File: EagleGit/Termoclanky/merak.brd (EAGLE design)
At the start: 160 x 100 mm, 14 parts

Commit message: Termoclanky: - koncept pcb
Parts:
- C1, C2, C5: device rcl:C050-035X075 -> rcl:C0805
- R1, R2, R3: device resistor:0207/12 -> resistor:R0805
- moved LED1 42.4 mm to (7.62, 59.7), turned to 270 degrees
- moved LED2 42.1 mm to (7.62, 54.6), turned to 270 degrees
- moved X2 15.9 mm to (35.6, 59.7), turned to 0 degrees
- moved R3 13.5 mm to (29.2, 48.3), flipped to the bottom, turned to 90 degrees
- moved C1 12.0 mm to (34.3, 40.6), flipped to the bottom
- moved R1 12.0 mm to (30.5, 33.0), flipped to the bottom, turned to 180 degrees
- moved R2 8.13 mm to (31.8, 48.3), flipped to the bottom, turned to 90 degrees
- moved C2 8.03 mm to (38.1, 33.0), flipped to the bottom, turned to 180 degrees
- moved C5 2.84 mm to (36.8, 48.3), flipped to the bottom, turned to 90 degrees
- moved C3 2.84 mm to (54.6, 47.0)
- moved C4 2.84 mm to (54.6, 35.6)
- moved X1 2.84 mm to (68.6, 40.6)
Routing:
- net GND: track 0.00 -> 125.9 mm, vias 0 -> 2
- net VDD: track 0.00 -> 112.3 mm
- net N$1: track 0.00 -> 37.1 mm
- net VSS: track 0.00 -> 33.2 mm
- net N$5: track 0.00 -> 28.9 mm
- net N$6: track 0.00 -> 24.2 mm
- net N$2: track 10.2 -> 16.1 mm
- net N$7: track 0.00 -> 2.86 mm
- net N$4: track 0.00 -> 2.86 mm

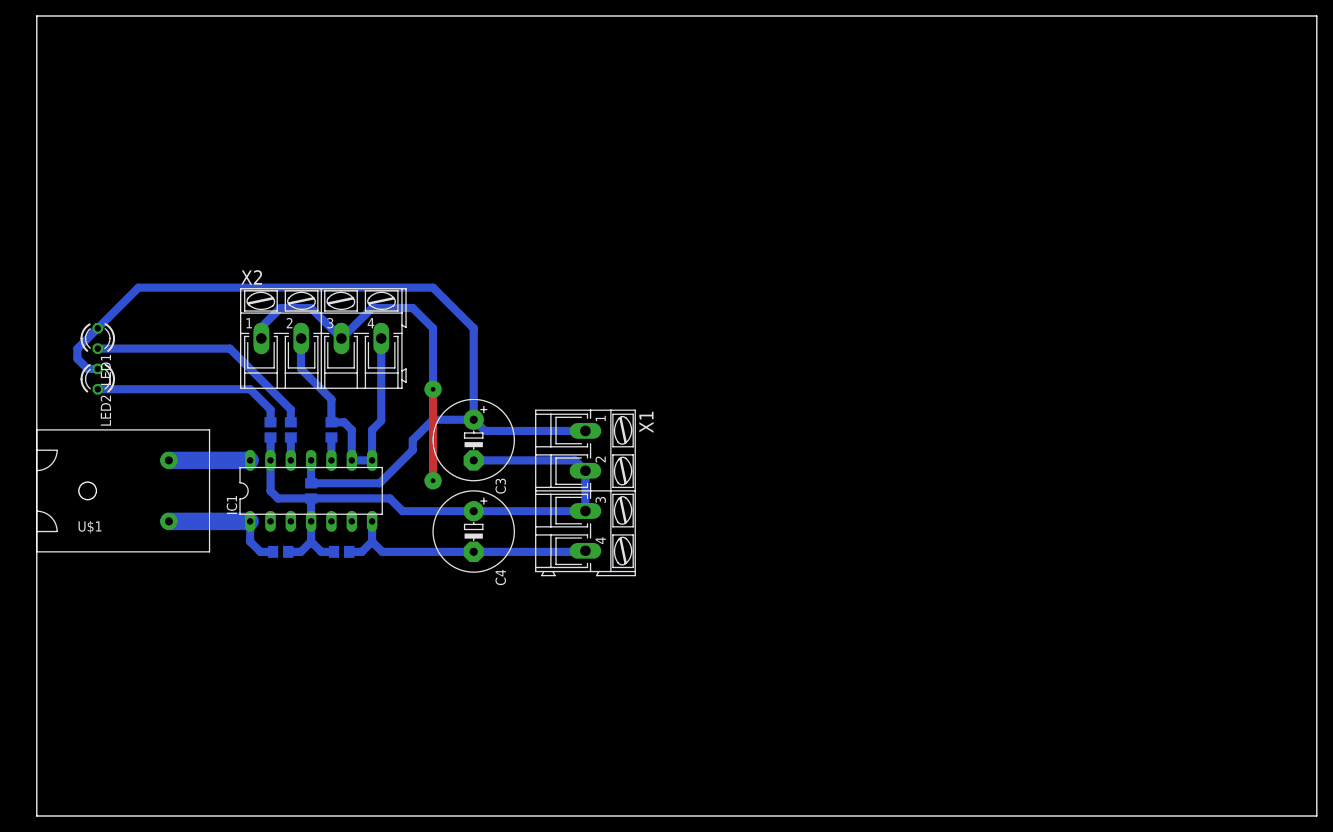
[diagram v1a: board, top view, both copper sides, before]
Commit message: Termoclanky: - hotova desticka meraku
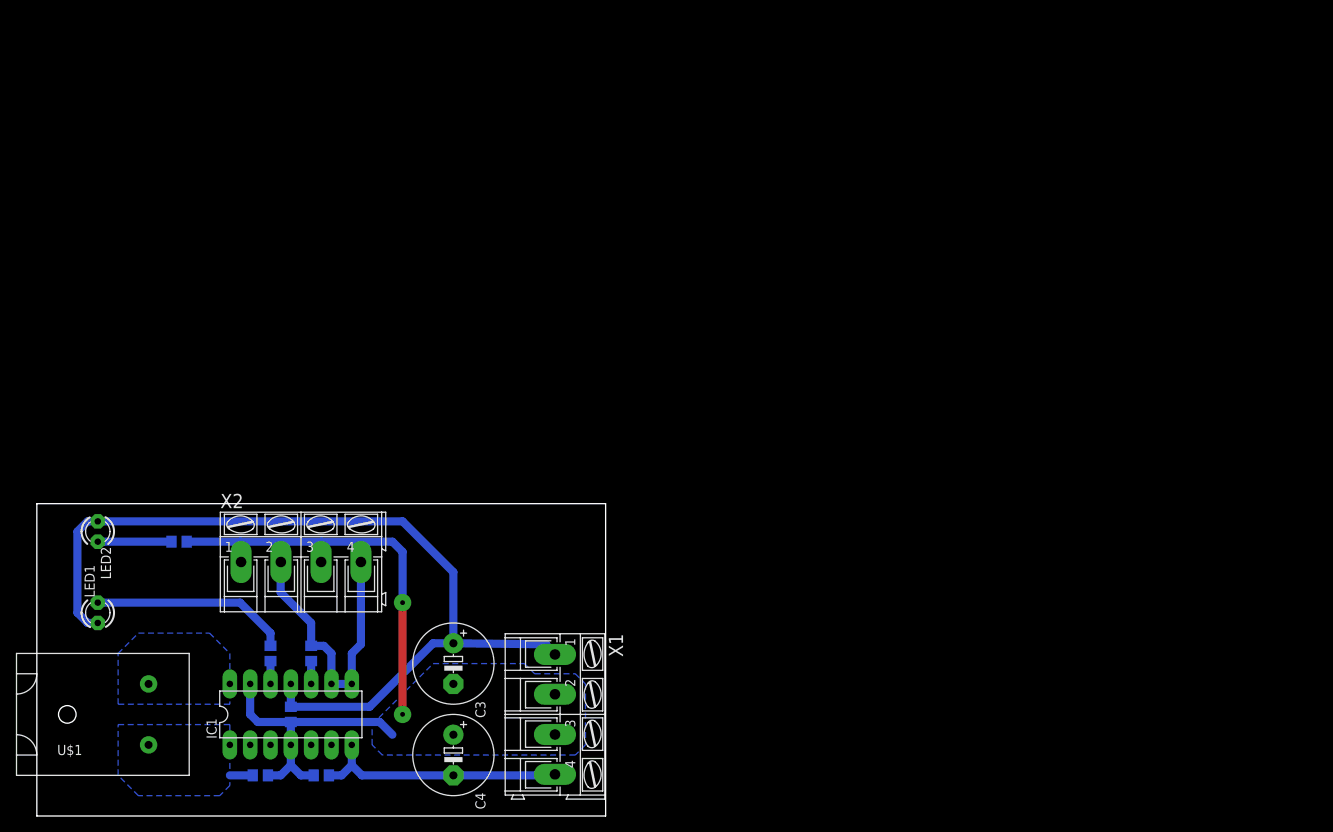
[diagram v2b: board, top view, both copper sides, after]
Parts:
- moved LED1 34.3 mm to (7.62, 25.4), turned to 90 degrees
- moved X1 28.2 mm to (64.8, 12.7)
- moved C2 28.1 mm to (35.6, 5.08)
- moved R1 28.1 mm to (27.9, 5.08)
- moved C1 28.1 mm to (31.8, 12.7)
- moved C3 28.1 mm to (52.1, 19.1)
- moved C4 28.1 mm to (52.1, 7.62)
- moved IC1 28.1 mm to (31.8, 12.7)
- moved U$1 28.1 mm to (11.4, 12.7)
- moved C5 28.1 mm to (34.3, 20.3)
- moved R2 28.1 mm to (29.2, 20.3)
- moved X2 28.1 mm to (33.0, 31.8)
- moved LED2 19.0 mm to (7.62, 35.6)
- moved R3 18.1 mm to (17.8, 34.3), turned to 0 degrees
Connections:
- net N$2 renamed PLUS
- net N$3 renamed MINUS
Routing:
- net GND: track 125.9 -> 87.8 mm
- net N$6: track 24.2 -> 9.21 mm
- net PLUS: track 16.1 -> 2.86 mm
- net MINUS: track 10.2 -> 0.00 mm
- net N$5: track 28.9 -> 24.8 mm
- net VSS: track 33.2 -> 31.9 mm
- added copper zone on layer 16, net GND
- added copper zone on layer 16, net MINUS
- added copper zone on layer 16, net PLUS
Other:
- board size 160 x 100 mm -> 71.1 x 39 mm

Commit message: Termoclanky + manuskript: - priprava do rtf
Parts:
- added U$2, U$3, U$4: (no value), holes:3,2
- C1, C2: value (none) -> 10n
- C3, C4: value (none) -> 10u; device rcl:E5-10,5 -> rcl:E2,5-5
- R1: value (none) -> 2k2
- moved X1 9.16 mm to (59.7, 20.3)
- moved C4 8.98 mm to (45.7, 14.0)
- moved C3 6.84 mm to (49.5, 25.4)
- moved LED1 5.68 mm to (5.08, 30.5)
- moved C1 5.08 mm to (31.8, 17.8)
- moved IC1 5.08 mm to (31.8, 17.8)
- moved U$1 5.08 mm to (11.4, 17.8)
- moved C2 5.08 mm to (35.6, 10.2)
- moved R1 5.08 mm to (27.9, 10.2)
- moved C5 5.08 mm to (34.3, 25.4)
- moved R2 5.08 mm to (29.2, 25.4)
- moved R3 3.81 mm to (17.8, 38.1)
- moved X2 3.81 mm to (33.0, 35.6)
- moved LED2 2.54 mm to (5.08, 35.6)
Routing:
- net VDD: track 112.0 -> 105.8 mm
- net VSS: track 31.9 -> 26.8 mm
- net GND: track 87.8 -> 83.0 mm
- net N$6: track 9.21 -> 13.3 mm
- net N$1: track 37.1 -> 34.5 mm
- net N$5: track 24.8 -> 27.3 mm
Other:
- board size 71.1 x 39 mm -> 66 x 42.2 mm
- board text added: "GND"
- board text added: "VDD"
- board text added: "VSS"

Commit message: Eagle: - Risa zdroj - Kovanda termoclanky - Quanti akcelerometr
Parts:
- LED1: value (none) -> ZLUTA
- LED2: value (none) -> CERVENA
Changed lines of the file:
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@@
 <layer number="46" name="Milling" color="3" fill="1" visible="no" active="yes"/>
 <layer number="47" name="Measures" color="7" fill="1" visible="no" active="yes"/>
-<layer number="48" name="Document" color="7" fill="1" visible="yes" active="yes"/>
-<layer number="49" name="Reference" color="7" fill="1" visible="yes" active="yes"/>
-<layer number="51" name="tDocu" color="7" fill="1" visible="yes" active="yes"/>
-<layer number="52" name="bDocu" color="7" fill="1" visible="yes" active="yes"/>
+<layer number="48" name="Document" color="7" fill="1" visible="no" active="yes"/>
+<layer number="49" name="Reference" color="7" fill="1" visible="no" active="yes"/>
+<layer number="51" name="tDocu" color="7" fill="1" visible="no" active="yes"/>
+<layer number="52" name="bDocu" color="7" fill="1" visible="no" active="yes"/>
 <layer number="90" name="Modules" color="5" fill="1" visible="no" active="no"/>
 <layer number="91" name="Nets" color="2" fill="1" visible="no" active="no"/>
@@
 <attribute name="OC_FARNELL" value="409194" x="31.75" y="17.78" size="1.778" layer="27" display="off"/>
 </element>
-<element name="LED1" library="led" package="LED3MM" value="" x="5.08" y="30.48" rot="R90"/>
-<element name="LED2" library="led" package="LED3MM" value="" x="5.08" y="35.56" rot="R270"/>
+<element name="LED1" library="led" package="LED3MM" value="ZLUTA" x="5.08" y="30.48" smashed="yes" rot="R90">
+<attribute name="NAME" x="13.335" y="30.099" size="1.27" layer="25" ratio="10" rot="R180"/>
+<attribute name="VALUE" x="13.335" y="28.321" size="1.27" layer="27" ratio="10" rot="R180"/>
+</element>
+<element name="LED2" library="led" package="LED3MM" value="CERVENA" x="5.08" y="35.56" smashed="yes" rot="R270">
+<attribute name="NAME" x="15.875" y="36.449" size="1.27" layer="25" ratio="10" rot="R180"/>
+<attribute name="VALUE" x="15.875" y="34.671" size="1.27" layer="27" ratio="10" rot="R180"/>
+</element>
 <element name="R1" library="resistor" package="R0805" value="2k2" x="27.94" y="10.16" rot="MR180"/>
 <element name="R2" library="resistor" package="R0805" value="2k2" x="29.21" y="25.4" rot="MR90"/>
@@
 <wire x1="26.99" y1="10.16" x2="24.13" y2="10.16" width="1.016" layer="16"/>
 <polygon width="0.6096" layer="16">
-<vertex x="10.16" y="16.51"/>
-<vertex x="24.13" y="16.51"/>
+<vertex x="10.16" y="17.145"/>
+<vertex x="24.13" y="17.145"/>
 <vertex x="24.13" y="8.89"/>
 <vertex x="22.86" y="7.62"/>
@@
 <contactref element="U$1" pad="MINUS"/>
 <polygon width="0.6096" layer="16">
-<vertex x="24.13" y="19.05"/>
-<vertex x="10.16" y="19.05"/>
+<vertex x="24.13" y="18.415"/>
+<vertex x="10.16" y="18.415"/>
 <vertex x="10.16" y="25.4"/>
 <vertex x="12.7" y="27.94"/>
